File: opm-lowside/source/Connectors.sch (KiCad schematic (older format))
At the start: 26 parts, among them J1 Current Sensing, J2 SPI/Info, J3 VCC_IO, J4 PWMx6, J5 Temperature, U1 TerminalBlock_2_P5.08mm, U2 TerminalBlock_3_P5.08mm

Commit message: first config
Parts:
- removed H201, H202: MountingHole, MountingHole:MountingHole_3.2mm_M3_Pad, symbol opm-cache:Mechanical_MountingHole_Pad
- added C29, C30, C31: 330uF/63V, Capacitor_THT:C_Radial_D10.0mm_H20.0mm_P5.00mm, symbol Device:CP1
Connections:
- net +VM: now also C29.1, C30.1, C31.1
- net GND: now also C29.2, C30.2, C31.2
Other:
- note removed: "Mountingholes"
- moved on the sheet: U1
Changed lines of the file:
@@
 $Descr A4 11693 8268
 encoding utf-8
-Sheet 3 3
+Sheet 2 3
 Title "opm-lowside"
 Date "2021-12-26"
@@
 Comment4 ""
 $EndDescr
-Wire Notes Line
-	7400 750  6400 750
-Wire Notes Line
-	7400 2150 7400 750
-Wire Notes Line
-	6400 2150 7400 2150
-Wire Notes Line
-	6400 750  6400 2150
-Text Notes 6450 900  0    79   ~ 0
-Mountingholes
-Connection ~ 6550 1300
-Wire Wire Line
-	6700 1300 6550 1300
-Wire Wire Line
-	6550 1100 6550 1300
-Wire Wire Line
-	6700 1100 6550 1100
-$Comp
-L power:GND #PWR0101
-U 1 1 5C336467
-P 6550 1850
-F 0 "#PWR0101" H 6550 1600 50  0001 C CNN
-F 1 "GND" H 6550 1700 50  0000 C CNN
-F 2 "" H 6550 1850 50  0001 C CNN
-F 3 "" H 6550 1850 50  0001 C CNN
-	1    6550 1850
-	1    0    0    -1
-$EndComp
-$Comp
-L opm-cache:Mechanical_MountingHole_Pad H?
-U 1 1 5C335D22
-P 6800 1300
-AR Path="/5C335D22" Ref="H?"  Part="1"
-AR Path="/5BA8C4E4/5C335D22" Ref="H202"  Part="1"
-F 0 "H202" V 6750 1450 39  0000 L CNN
-F 1 "MountingHole" V 6800 1450 39  0000 L CNN
-F 2 "MountingHole:MountingHole_3.2mm_M3_Pad" H 6800 1300 39  0001 C CNN
-F 3 "~" H 6800 1300 39  0001 C CNN
-F 4 "No" V 6800 1300 50  0001 C CNN "JLCPCB BOM"
-	1    6800 1300
-	0    1    1    0
-$EndComp
-$Comp
-L opm-cache:Mechanical_MountingHole_Pad H?
-U 1 1 5C33535A
-P 6800 1100
-AR Path="/5C33535A" Ref="H?"  Part="1"
-AR Path="/5BA8C4E4/5C33535A" Ref="H201"  Part="1"
-F 0 "H201" V 6750 1250 39  0000 L CNN
-F 1 "MountingHole" V 6800 1250 39  0000 L CNN
-F 2 "MountingHole:MountingHole_3.2mm_M3_Pad" H 6800 1100 39  0001 C CNN
-F 3 "~" H 6800 1100 39  0001 C CNN
-F 4 "No" V 6800 1100 50  0001 C CNN "JLCPCB BOM"
-	1    6800 1100
-	0    1    1    0
-$EndComp
 Wire Notes Line
 	3400 750  3400 2150
@@
 L opm-cache:Conector_library_Metz_31330102 U1
 U 1 1 61BFF192
-P 1500 1300
-F 0 "U1" H 1500 1100 39  0000 C CNN
-F 1 "TerminalBlock_2_P5.08mm" H 1500 1150 39  0000 C CNN
-F 2 "Libraries:TerminalBlock_bornier-2_P5.08mm" H 1500 1150 39  0001 C CNN
-F 3 "https://datasheet.lcsc.com/lcsc/1912251636_Ningbo-Kangnex-Elec-WJ500V-5-08-2P_C8465.pdf" H 1550 1300 39  0001 C CNN
-F 4 "C8465" H 1500 1300 50  0001 C CNN "LCSC"
-F 5 "WJ500V-5.08-2P" H 1500 1300 50  0001 C CNN "manf_num"
-	1    1500 1300
+P 750 1300
+F 0 "U1" H 750 1100 39  0000 C CNN
+F 1 "TerminalBlock_2_P5.08mm" H 750 1150 39  0000 C CNN
+F 2 "Libraries:TerminalBlock_bornier-2_P5.08mm" H 750 1150 39  0001 C CNN
+F 3 "https://datasheet.lcsc.com/lcsc/1912251636_Ningbo-Kangnex-Elec-WJ500V-5-08-2P_C8465.pdf" H 800 1300 39  0001 C CNN
+F 4 "C8465" H 750 1300 50  0001 C CNN "LCSC"
+F 5 "WJ500V-5.08-2P" H 750 1300 50  0001 C CNN "manf_num"
+	1    750  1300
 	-1   0    0    1
 $EndComp
 Wire Wire Line
-	1700 1350 1600 1350
+	950  1350 850  1350
 $Comp
 L Device:CP1 C4
@@
 	2850 1350 2850 1250
 Wire Wire Line
-	2850 1250 2350 1250
-Wire Wire Line
-	2350 1250 2350 1350
-Wire Wire Line
 	2350 1650 2350 1750
 Wire Wire Line
@@
 Wire Wire Line
 	2850 1750 2850 1650
-Connection ~ 2350 1250
 $Comp
 L power:GND #PWR0105
@@
 Connection ~ 2850 1750
 Wire Wire Line
-	1700 1350 1700 1750
-Connection ~ 2350 1750
+	950  1350 950  1750
 Wire Wire Line
 	2850 1250 3100 1250
@@
 Wire Wire Line
 	4100 3000 4400 3000
-Wire Wire Line
-	6550 1300 6550 1850
 Wire Notes Line
 	3500 3750 6300 3750
@@
 Text HLabel 1350 6550 0    50   Input ~ 0
 ADC_I_w
-Wire Wire Line
-	1600 1250 2350 1250
-Wire Wire Line
-	1700 1750 2350 1750
 $Comp
 L Connector:Conn_01x06_Female J2
@@
 Text HLabel 1400 5500 0    50   Input ~ 0
 SPI1_MOSI
+$Comp
+L Device:CP1 C29
+U 1 1 61C9E9C9
+P 1150 1500
+F 0 "C29" V 1000 1500 39  0000 C CNN
+F 1 "330uF/63V" V 1300 1500 39  0000 C CNN
+F 2 "Capacitor_THT:C_Radial_D10.0mm_H20.0mm_P5.00mm" V 1350 1500 39  0001 C CNN
+F 3 "~" H 1150 1500 39  0001 C CNN
+F 4 "C338235" V 1150 1500 50  0001 C CNN "LCSC"
+F 5 "63ZLH330MEFC10X23" V 1150 1500 50  0001 C CNN "manf_num"
+	1    1150 1500
+	1    0    0    -1
+$EndComp
+$Comp
+L Device:CP1 C30
+U 1 1 61C9F5FE
+P 1550 1500
+F 0 "C30" V 1400 1500 39  0000 C CNN
+F 1 "330uF/63V" V 1700 1500 39  0000 C CNN
+F 2 "Capacitor_THT:C_Radial_D10.0mm_H20.0mm_P5.00mm" V 1750 1500 39  0001 C CNN
+F 3 "~" H 1550 1500 39  0001 C CNN
+F 4 "C338235" V 1550 1500 50  0001 C CNN "LCSC"
+F 5 "63ZLH330MEFC10X23" V 1550 1500 50  0001 C CNN "manf_num"
+	1    1550 1500
+	1    0    0    -1
+$EndComp
+$Comp
+L Device:CP1 C31
+U 1 1 61C9FE15
+P 2000 1500
+F 0 "C31" V 1850 1500 39  0000 C CNN
+F 1 "330uF/63V" V 2150 1500 39  0000 C CNN
+F 2 "Capacitor_THT:C_Radial_D10.0mm_H20.0mm_P5.00mm" V 2200 1500 39  0001 C CNN
+F 3 "~" H 2000 1500 39  0001 C CNN
+F 4 "C338235" V 2000 1500 50  0001 C CNN "LCSC"
+F 5 "63ZLH330MEFC10X23" V 2000 1500 50  0001 C CNN "manf_num"
+	1    2000 1500
+	1    0    0    -1
+$EndComp
+Wire Wire Line
+	950  1750 1150 1750
+Connection ~ 2350 1750
+Wire Wire Line
+	850  1250 1150 1250
+Wire Wire Line
+	2350 1350 2350 1250
+Connection ~ 2350 1250
+Wire Wire Line
+	2350 1250 2850 1250
+Wire Wire Line
+	1550 1350 1550 1250
+Connection ~ 1550 1250
+Wire Wire Line
+	1550 1250 2000 1250
+Wire Wire Line
+	2000 1350 2000 1250
+Connection ~ 2000 1250
+Wire Wire Line
+	2000 1250 2350 1250
+Wire Wire Line
+	2000 1650 2000 1750
+Connection ~ 2000 1750
+Wire Wire Line
+	2000 1750 2350 1750
+Wire Wire Line
+	1550 1650 1550 1750
+Connection ~ 1550 1750
+Wire Wire Line
+	1550 1750 2000 1750
+Wire Wire Line
+	1150 1650 1150 1750
+Connection ~ 1150 1750
+Wire Wire Line
+	1150 1750 1550 1750
+Wire Wire Line
+	1150 1350 1150 1250
+Connection ~ 1150 1250
+Wire Wire Line
+	1150 1250 1550 1250
 $EndSCHEMATC

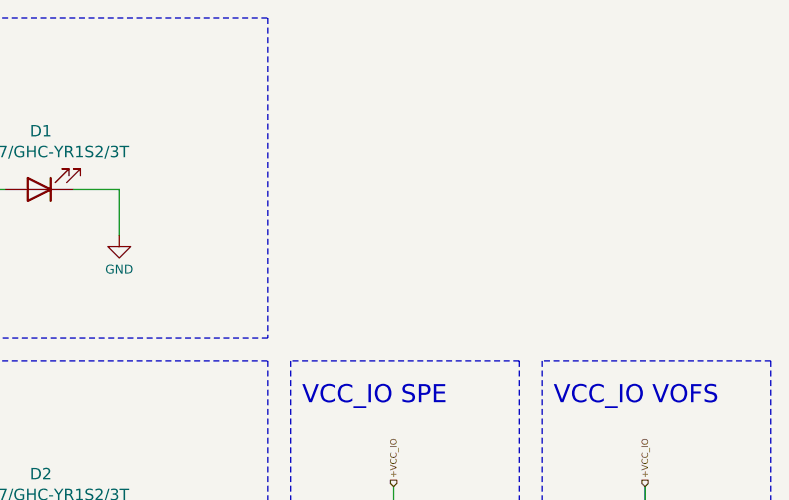
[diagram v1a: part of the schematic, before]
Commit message: add heatsink
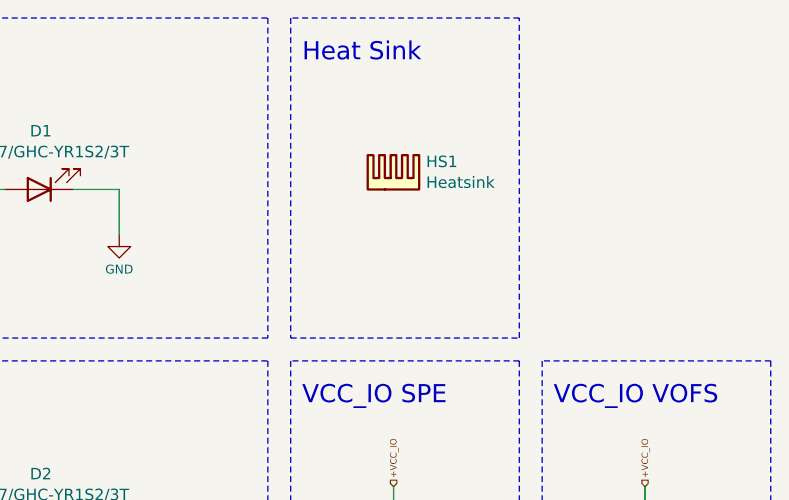
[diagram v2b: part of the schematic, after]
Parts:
- added HS1: Heatsink, Libraries:Heatsink_30x30mm_2xFixation3mm, symbol Mechanical:Heatsink
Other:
- note added: "Heat Sink"
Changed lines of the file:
@@
 Wire Wire Line
 	1150 1250 1550 1250
+Wire Notes Line
+	6400 750  6400 2150
+Wire Notes Line
+	6400 2150 7400 2150
+Wire Notes Line
+	7400 2150 7400 750
+Wire Notes Line
+	7400 750  6400 750
+Text Notes 6450 950  0    79   ~ 0
+Heat Sink
+$Comp
+L Mechanical:Heatsink HS1
+U 1 1 61D1CBEC
+P 6850 1500
+F 0 "HS1" H 6992 1621 50  0000 L CNN
+F 1 "Heatsink" H 6992 1530 50  0000 L CNN
+F 2 "Libraries:Heatsink_30x30mm_2xFixation3mm" H 6862 1500 50  0001 C CNN
+F 3 "~" H 6862 1500 50  0001 C CNN
+	1    6850 1500
+	1    0    0    -1
+$EndComp
 $EndSCHEMATC

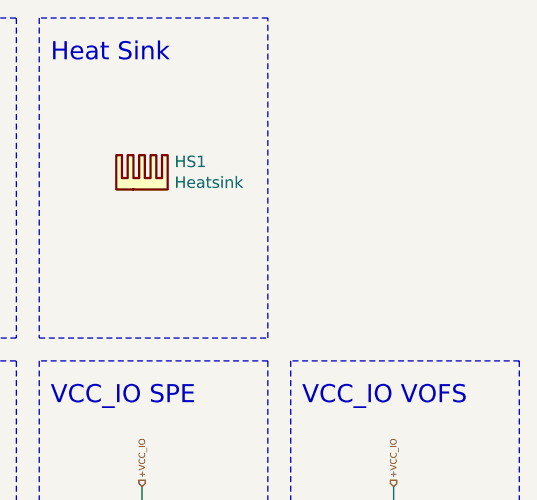
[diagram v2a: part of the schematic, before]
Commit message: add fan
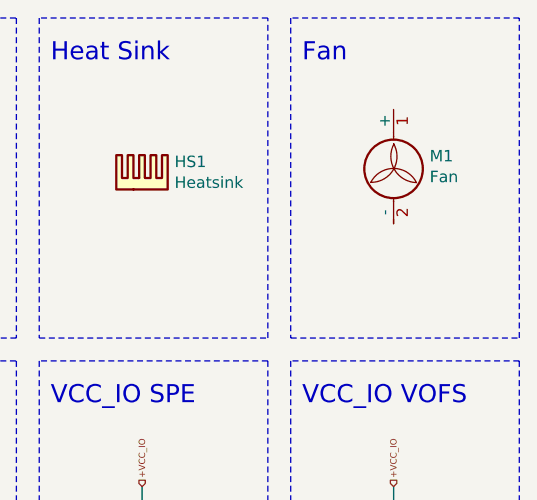
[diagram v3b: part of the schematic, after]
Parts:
- added M1: Fan, Libraries:Fan_3010, symbol Motor:Fan
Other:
- note added: "Fan"
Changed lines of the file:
@@
+	1    0    0    -1
+$EndComp
+Wire Notes Line
+	7500 750  7500 2150
+Wire Notes Line
+	7500 2150 8500 2150
+Wire Notes Line
+	8500 2150 8500 750
+Wire Notes Line
+	8500 750  7500 750
+Text Notes 7550 950  0    79   ~ 0
+Fan
+$Comp
+L Motor:Fan M1
+U 1 1 61D527C4
+P 7950 1450
+F 0 "M1" H 8108 1546 50  0000 L CNN
+F 1 "Fan" H 8108 1455 50  0000 L CNN
+F 2 "Libraries:Fan_3010" H 7950 1460 50  0001 C CNN
+F 3 "~" H 7950 1460 50  0001 C CNN
+	1    7950 1450
 	1    0    0    -1
 $EndComp

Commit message: update position
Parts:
- U2: LCSC C72334 -> (none)
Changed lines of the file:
@@
 F 1 "TerminalBlock_3_P5.08mm" H 2400 2900 39  0000 C CNN
 F 2 "Libraries:TerminalBlock_bornier-3_P5.08mm" H 2400 2350 39  0001 C CNN
-F 3 "https://datasheet.lcsc.com/lcsc/1912251709_Ningbo-Kangnex-Elec-WJ500V-5-08-3P_C72334.pdf" H 2450 2650 39  0001 C CNN
-F 4 "C72334" H 2400 2700 50  0001 C CNN "LCSC"
+F 3 "" H 2450 2650 39  0001 C CNN
+F 4 "" H 2400 2700 50  0001 C CNN "LCSC"
 F 5 "WJ500V-5.08-3P" H 2400 2700 50  0001 C CNN "manf_num"
 	1    2400 2700
